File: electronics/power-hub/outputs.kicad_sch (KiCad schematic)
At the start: 76 parts, among them J2 ROW A, J3 ROW B, J4 ROW C, J5 ROW D, U11 TPS26600PWPR, U12 TPS26600PWPR, U13 TPS26600PWPR, U14 TPS26600PWPR

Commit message: Datasheet audit F1-F6: the pod's AP2114H, STB 5.1k, PC_DET hysteresis, the camera ESD's 100 nF, the eFuse step
The user approved the audit's fixes for the node, the hub and the pod
("Go pour 1"); docs/datasheet-audit.md marks F1-F6 applied.

* F1, camera pod: U1 AMS1117-3.3 -> AP2114H-3.3TRG1 (C150716, catalog
  ldo_1a, the node's U2).
  - The AMS1117 is specified stable only with 22 uF tantalum; the
    AP2114H is stable with the ceramic C2.
  - Same SOT-223 pinout, copper (the +3V3 pour and island round the
    tab stay) and 180 deg CPL correction.
  - One more extended type on the pod's Economic order: +$3.09 and
    $0.05 of parts (JLC_SINCE_QUOTE).
* F2, power hub: R214 (TJA1462 STB pull-down) 10k -> 5.1k (C23186,
  already on the board). With IO9 floating, STB's internal pull-up
  (20 kOhm minimum) left it at up to 1.10 V, over VIL 0.99 V.
* F3, bay node: R42 150k from MUX_SEL back to PC_DET, beside U7 (C22807,
  on the board since S1).
  - The laptop's VBUS rises at ~50 us/V through R11/R12, where the
    LVC1G32 wants <= 10 ns/V and warns of oscillation.
  - This gives ~0.14 V of hysteresis.
* F4, bay node: C28 100 nF (C14663) on U12/U13's VBUS pins (+3V3), above
  U12 by its pin 5. Between the two ICs their courtyards leave no room.
* F5, node and hub: firmware.md's first-flash procedure gains the
  irreversible DIS_USB_OTG_DOWNLOAD_MODE eFuse step. In USB-OTG
  download boot the ROM drives IO40 high: the node's DUT_FLT_N, the
  hub's PD_SCL. Nothing is burnt.
* F6, notes, hub:
  - the IMON filter is 0.9 ms, not 47 us: the pin is a current source;
  - the buck stops at ~3.8 V (internal UVLO);
  - SHDN turns on at >= 1 V;
  - the soft start stays under the limit only typically;
  - the CH224A note follows CH224 V2.1: the source PDOs are listed for
    both parts and readable under 100 W, which is still to check with
    ours (review R3); single-byte transfers; no "same die".
* F6, notes, node: TPS2553D; the LDO's 1.94 V x 0.4 A ~ 0.8 W; L1's
  7.5 A guarante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
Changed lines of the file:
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@@
 		)
 	)
-	(text_box "TPS26600: I_LIM ≈ 12 A·kΩ / R_ILIM → 7.5k ≈ 1.6 A (JST PH: 2 A per contact).\nt_dVdT = 8e3 · V_IN · C_dVdT → 47 nF ≈ 7.5 ms at 20 V, 10.5 ms at 28 V.  A row of four nodes (≈ 450 µF)\n  then charges at C / (8e3 · C_dVdT) ≈ 1.2 A, under the 1.6 A limit (22 nF needed ≈ 2.6 A).\nIMON: 78 µA/A into 18k → 1.4 V/A (2.2 V at the limit), 1k + 47 nF (47 µs) to the ESP32's ADC.\nSHDN: 10k to GND (row off: ≤ 10 µA from the pin, 0.1 V), ROW_EN through 10k → 1.65 V (on above 0.94 V).\nThe firmware holds ROW_EN with the ESP32's GPIO hold, so a controller reset leaves the rows as they were.\nFLT: open drain, 100k to 3.3 V for the controller; the red LED (1k) is fed from ROW_EN: it lights only for\n  a fault on an enabled row (FLT is also low while a row is off or starting).\nD41–D44 B5819W: GND → each row's output at its connector, for the cable's kick when the eFuse cuts a short.\nUVLO / OVP / MODE to GND: internal 15 V / 31–34 V (typ 32.6 V) thresholds, current-limit mode, auto-retry."
+	(text_box "TPS26600: I_LIM ≈ 12 A·kΩ / R_ILIM → 7.5k ≈ 1.6 A (JST PH: 2 A per contact).\nt_dVdT = 8e3 · V_IN · C_dVdT → 47 nF ≈ 7.5 ms at 20 V, 10.5 ms at 28 V.  A row of four nodes (≈ 450 µF)\n  then charges at C / (8e3 · C_dVdT) ≈ 1.2 A typically, under the 1.6 A limit (22 nF needed ≈ 2.6 A); at the\n  corners (+20 % capacitance, a fast dVdT, the nodes' load, the limit at its 1.5 A minimum) a row starts in current limit.\nIMON: 78 µA/A into 18k → 1.4 V/A (2.2 V at the limit), 1k + 47 nF to the ESP32's ADC: the pin is a current\n  source, so τ = (18k + 1k) × 47 nF ≈ 0.9 ms, against the firmware's 250 ms polling.\nSHDN: 10k to GND (row off: ≤ 10 µA from the pin, 0.1 V), ROW_EN through 10k → 1.65 V (TI: ≥ 1 V to turn on, p. 26).\nThe firmware holds ROW_EN with the ESP32's GPIO hold, so a controller reset leaves the rows as they were.\nFLT: open drain, 100k to 3.3 V for the controller; the red LED (1k) is fed from ROW_EN: it lights only for\n  a fault on an enabled row (FLT is also low while a row is off or starting).\nD41–D44 B5819W: GND → each row's output at its connector, for the cable's kick when the eFuse cuts a short.\nUVLO / OVP / MODE to GND: internal 15 V / 31–34 V (typ 32.6 V) thresholds, current-limit mode, auto-retry."
 		(exclude_from_sim no)
 		(at 20.32 353.06 0)
-		(size 414.02 26.67)
+		(size 414.02 31.75)
 		(margins 1.5 1.5 1.5 1.5)
 		(stroke

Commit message: Boards: labelled bottom test pads; hub dVdT 100 nF, 50 ms FLT blank
Eve's DFT rule on the four boards this session owns: bare pads on the
bottom, named on B.SilkS, out of the BOM and the CPL (no part, no
assembly fee).  Supply pads 1.5 mm, signal pads 1.0 mm (new catalog
entry "testpad1"), all more than 2 mm from any THT pad or hole
(closest: 4.7 mm, the pod's TP4).  Positions are fixed in design.py,
so they stay put across revisions.

- bay node, 17: TX, RX, 3V3, GND by the module (kept), then EN, IO0,
  FLT (DUT_FLT_N), ALRT (INA_ALERT_N), SDA, SCL and a second GND;
  a supply row along the bottom edge: GND, VIN, 5V, 3V3, DUT 5V,
  CAM 5V
- power hub, 20: TX, RX, 3V3, GND, 5V, VRACK, GND (kept), then EN,
  IO0, the CH224A's PD SDA/SCL, each row's FLT and IMON (A-D) and a
  third GND in the middle
- camera pod, 4: GND, 5V, 3V3 and a second GND at the far end
- DATA port, 2: GND and 5V (VBUS, through a via under its track)

Hub, as the datasheet audit's U1 answer asks (TPS2660 Fig. 55 at
85 C: 8-10 ms at 21 W fails the 47 nF worst start, 33 ms at 14 W
covers 100 nF): C21-C24 dVdT 47 nF -> 100 nF, so a row's soft start
is 16-22 ms and dissipates about 7-9 W typical, 14 W worst, for
19-24 ms; the firmware's HUB_ROW_FLT_BLANK_MS goes 25 -> 50 ms to
cover it (worst case 39 ms).  docs/power.md, the audit row and the
hub notes say so.

Routing fallout: J1's A12/B1 GND now leaves through one drawn 0.5 mm
via so the automatic fan-out can't cut the VRACK pour off A9/B4; the
pod's LDO tab zones are exclusive so tracks no longer split them.

All four rerouted, tidied and checked: ERC 0, DRC 0, unconnected 0,
parity 0.  Gerbers, renders, schematics, viewer GLBs, the JLC
snapshot lines and the rack BOM regenerated.

Co-Authored-By: Claude Opus 5.5 <noreply@anthropic.com>
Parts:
- C21, C22, C23, C24: value 47n -> 100n; LCSC C1622 -> C14663; MPN CL10B473KB8NNNC -> CC0603KRX7R9BB104; Manufacturer Samsung Electro-Mechanics -> YAGEO
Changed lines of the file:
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@@
 			)
 		)
-		(property "Value" "47n"
+		(property "Value" "100n"
 			(at 120.65 71.12 0)
 			(effects
@@
 			)
 		)
-		(property "Description" "Capacitor 47n 0603"
+		(property "Description" "Capacitor 100n 0603"
 			(at 116.84 73.66 0)
 			(effects
@@
 			)
 		)
-		(property "LCSC" "C1622"
+		(property "LCSC" "C14663"
 			(at 116.84 73.66 0)
 			(effects
@@
 			)
 		)
-		(property "MPN" "CL10B473KB8NNNC"
+		(property "MPN" "CC0603KRX7R9BB104"
 			(at 116.84 73.66 0)
 			(effects
@@
 			)
 		)
-		(property "Manufacturer" "Samsung Electro-Mechanics"
+		(property "Manufacturer" "YAGEO"
 			(at 116.84 73.66 0)
 			(effects
@@
 			)
 		)
-		(property "Value" "47n"
+		(property "Value" "100n"
 			(at 120.65 151.13 0)
 			(effects
@@
 			)
 		)
-		(property "Description" "Capacitor 47n 0603"
+		(property "Description" "Capacitor 100n 0603"
 			(at 116.84 153.67 0)
 			(effects
@@
 			)
 		)
-		(property "LCSC" "C1622"
+		(property "LCSC" "C14663"
 			(at 116.84 153.67 0)
 			(effects
@@
 			)
 		)
-		(property "MPN" "CL10B473KB8NNNC"
+		(property "MPN" "CC0603KRX7R9BB104"
 			(at 116.84 153.67 0)
 			(effects
@@
 			)
 		)
-		(property "Manufacturer" "Samsung Electro-Mechanics"
+		(property "Manufacturer" "YAGEO"
 			(at 116.84 153.67 0)
 			(effects
@@
 			)
 		)
-		(property "Value" "47n"
+		(property "Value" "100n"
 			(at 120.65 232.41 0)
 			(effects
@@
 			)
 		)
-		(property "Description" "Capacitor 47n 0603"
+		(property "Description" "Capacitor 100n 0603"
 			(at 116.84 234.95 0)
 			(effects
@@
 			)
 		)
-		(property "LCSC" "C1622"
+		(property "LCSC" "C14663"
 			(at 116.84 234.95 0)
 			(effects
@@
 			)
 		)
-		(property "MPN" "CL10B473KB8NNNC"
+		(property "MPN" "CC0603KRX7R9BB104"
 			(at 116.84 234.95 0)
 			(effects
@@
 			)
 		)
-		(property "Manufacturer" "Samsung Electro-Mechanics"
+		(property "Manufacturer" "YAGEO"
 			(at 116.84 234.95 0)
 			(effects
@@
 			)
 		)
-		(property "Value" "47n"
+		(property "Value" "100n"
 			(at 120.65 312.42 0)
 			(effects
@@
 			)
 		)
-		(property "Description" "Capacitor 47n 0603"
+		(property "Description" "Capacitor 100n 0603"
 			(at 116.84 314.96 0)
 			(effects
@@
 			)
 		)
-		(property "LCSC" "C1622"
+		(property "LCSC" "C14663"
 			(at 116.84 314.96 0)
 			(effects
@@
 			)
 		)
-		(property "MPN" "CL10B473KB8NNNC"
+		(property "MPN" "CC0603KRX7R9BB104"
 			(at 116.84 314.96 0)
 			(effects
@@
 			)
 		)
-		(property "Manufacturer" "Samsung Electro-Mechanics"
+		(property "Manufacturer" "YAGEO"
 			(at 116.84 314.96 0)
 			(effects
@@
 		)
 	)
-	(text_box "TPS26600: I_LIM ≈ 12 A·kΩ / R_ILIM → 7.5k ≈ 1.6 A (JST PH: 2 A per contact).\nt_dVdT = 8e3 · V_IN · C_dVdT → 47 nF ≈ 7.5 ms at 20 V, 10.5 ms at 28 V.  A row of four nodes (≈ 450 µF)\n  then charges at C / (8e3 · C_dVdT) ≈ 1.2 A typically, under the 1.6 A limit (22 nF needed ≈ 2.6 A); at the\n  corners (+20 % capacitance, a fast dVdT, the nodes' load, the limit at its 1.5 A minimum) a row starts in current limit.\nIMON: 78 µA/A into 18k → 1.4 V/A (2.2 V at the limit), 1k + 47 nF to the ESP32's ADC: the pin is a current\n  source, so τ = (18k + 1k) × 47 nF ≈ 0.9 ms, against the firmware's 250 ms polling.\nSHDN: 10k to GND (row off: ≤ 10 µA from the pin, 0.1 V), ROW_EN through 10k → 1.65 V (TI: ≥ 1 V to turn on, p. 26).\nThe firmware holds ROW_EN with the ESP32's GPIO hold, so a controller reset leaves the rows as they were.\nFLT: open drain, 100k to 3.3 V for the controller; the red LED (1k) is fed from ROW_EN: it lights only for\n  a fault on an enabled row (FLT is also low while a row is off or starting).\nD41–D44 B5819W: GND → each row's output at its connector, for the cable's kick when the eFuse cuts a short.\nUVLO / OVP / MODE to GND: internal 15 V / 31–34 V (typ 32.6 V) thresholds, current-limit mode, auto-retry."
+	(text_box "TPS26600: I_LIM ≈ 12 A·kΩ / R_ILIM → 7.5k ≈ 1.6 A (JST PH: 2 A per contact).\nt_dVdT = 8e3 · V_IN · C_dVdT → 100 nF ≈ 16 ms at 20 V, 22 ms at 28 V.  A row of four nodes (≈ 450 µF) then\n  charges at C / (8e3 · C_dVdT) ≈ 0.56 A (≤ 1.3 A at the corners with the nodes' load), under the 1.6 A limit.\n  The eFuse takes ≈ 7–9 W typically, ≈ 14 W worst, for 19–24 ms: TI Fig. 55 with its 30 % margin (47 nF: ≈ 21 W, 12 ms).\nIMON: 78 µA/A into 18k → 1.4 V/A (2.2 V at the limit), 1k + 47 nF to the ESP32's ADC: the pin is a current\n  source, so τ = (18k + 1k) × 47 nF ≈ 0.9 ms, against the firmware's 250 ms polling.\nSHDN: 10k to GND (row off: ≤ 10 µA from the pin, 0.1 V), ROW_EN through 10k → 1.65 V (TI: ≥ 1 V to turn on, p. 26).\nThe firmware holds ROW_EN with the ESP32's GPIO hold, so a controller reset leaves the rows as they were.\nFLT: open drain, 100k to 3.3 V for the controller; the red LED (1k) is fed from ROW_EN: it lights only for\n  a fault on an enabled row (FLT is also low while a row is off or starting).\nD41–D44 B5819W: GND → each row's output at its connector, for the cable's kick when the eFuse cuts a short.\nUVLO / OVP / MODE to GND: internal 15 V / 31–34 V (typ 32.6 V) thresholds, current-limit mode, auto-retry."
 		(exclude_from_sim no)
 		(at 20.32 353.06 0)

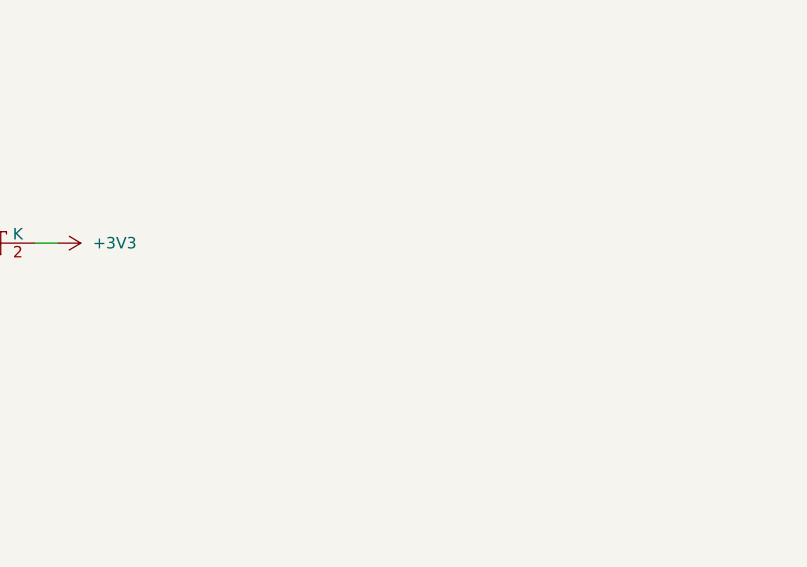
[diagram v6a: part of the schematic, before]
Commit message: Power hub: 18 more labelled bottom test pads (PH-2)
The kicad-happy review's PH-2, against Eve's rule: three bring-up
checks had no probe point (the +5V_BUCK load step, a row's output
during a short, the CAN common mode).  TP21-TP38, bare pads on B.Cu
named on B.SilkS, out of the BOM and the CPL:
- 1.5 mm: 5V BUCK, USB 5V, VHV (the CH224A's), ROW A-D, and a GND by
  the CAN pads;
- 1.0 mm: PD PG (PD_INT), CANH, CANL, TXD, RXD, EN A-D (ROW_EN), VSNS
  (VBUS_SENSE).

Each pad sits where its net already is, so no routing moves:
- 7 on a new drawn via, on one of the net's F.Cu track bends or in
  its pour (5V BUCK, USB 5V, VHV, PD PG, TXD, RXD, GND);
- 5 on a via the router had put there, now drawn so it stays
  (CANH, EN A-D);
- the 4 rows on their own drawn output vias;
- 2 on the end of a B.Cu track (CANL, VSNS).
None adds a via on In2's VRACK band.  All are at least 2 mm from any
through-hole pad or hole, and 2.7 mm from each other.  The GND pad
gets the usual GND fan-out to In1.  Positions are in TP_ROUND2 in
design.py.

Every track and via is the previous commit's, but those.  ERC 0,
DRC 0, unconnected 0, parity 0.

Co-Authored-By: Claude Opus 5.5 <noreply@anthropic.com>
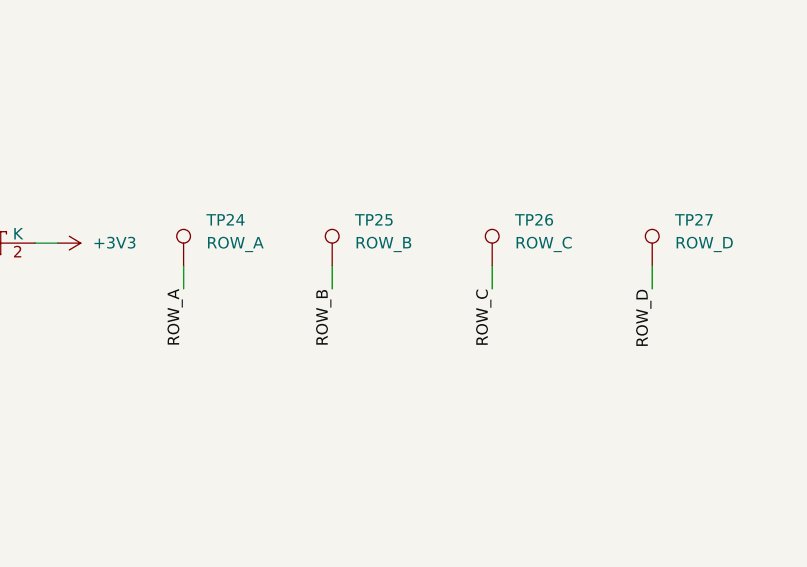
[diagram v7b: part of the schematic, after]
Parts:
- added TP24: ROW_A, TestPoint:TestPoint_Pad_D1.5mm, symbol Connector:TestPoint
- added TP25: ROW_B, TestPoint:TestPoint_Pad_D1.5mm, symbol Connector:TestPoint
- added TP26: ROW_C, TestPoint:TestPoint_Pad_D1.5mm, symbol Connector:TestPoint
- added TP27: ROW_D, TestPoint:TestPoint_Pad_D1.5mm, symbol Connector:TestPoint
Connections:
- net ROW_A: now also TP24.1
- net ROW_B: now also TP25.1
- net ROW_C: now also TP26.1
- net ROW_D: now also TP27.1
